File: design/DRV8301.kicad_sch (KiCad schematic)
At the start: 37 parts, among them U2 LM3671, U3 DRV8301

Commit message: Agregue LCSC Part #
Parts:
- L2: MPN LQM18DN220M70L -> (none); Manufacturer Murata Electronics -> APV
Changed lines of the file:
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@@
 			)
 		)
-		(property "Description" "600mA 2.2uH ±20% 300mΩ 0603 Inductors "
+		(property "Description" "600mA 2.2uH ±20% 300mΩ 0603 Inductors"
 			(at 120.65 147.32 0)
 			(effects
@@
 			)
 		)
-		(property "Manufacturer" "Murata Electronics"
+		(property "Manufacturer" "APV"
 			(at 194.31 50.8 0)
 			(effects
@@
 			)
 		)
-		(property "MPN" "LQM18DN220M70L"
+		(property "MPN" ""
 			(at 194.31 50.8 0)
 			(effects

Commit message: Agregue LCSC Part # a algunas resistencias
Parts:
- R10, R11, R9: LCSC (none) -> C163424
- R12, R14, R15: LCSC (none) -> C227479
- R13: LCSC (none) -> C6769250
- R4: LCSC (none) -> C108078
- R5: LCSC (none) -> C309650
- R6: LCSC (none) -> C114661
- R7: LCSC (none) -> C98220
- R8: LCSC (none) -> C123420
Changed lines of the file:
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@@
 			)
 		)
+		(property "LCSC" "C123420"
+			(at 119.38 29.21 0)
+			(effects
+				(font
+					(size 1.27 1.27)
+				)
+				(hide yes)
+			)
+		)
 		(pin "2"
 		)
@@
 			)
 		)
+		(property "LCSC" "C309650"
+			(at 85.09 36.83 0)
+			(effects
+				(font
+					(size 1.27 1.27)
+				)
+				(hide yes)
+			)
+		)
 		(pin "2"
 		)
@@
 			)
 		)
+		(property "LCSC" "C108078"
+			(at 85.09 26.67 0)
+			(effects
+				(font
+					(size 1.27 1.27)
+				)
+				(hide yes)
+			)
+		)
 		(pin "2"
 		)
@@
 			)
 		)
+		(property "LCSC" "C114661"
+			(at 99.06 35.56 0)
+			(effects
+				(font
+					(size 1.27 1.27)
+				)
+				(hide yes)
+			)
+		)
 		(pin "1"
 		)
@@
 			)
 		)
+		(property "LCSC" "C163424"
+			(at 240.03 101.6 0)
+			(effects
+				(font
+					(size 1.27 1.27)
+				)
+				(hide yes)
+			)
+		)
 		(pin "1"
 		)
@@
 			)
 		)
+		(property "LCSC" "C227479"
+			(at 250.19 106.68 0)
+			(effects
+				(font
+					(size 1.27 1.27)
+				)
+				(hide yes)
+			)
+		)
 		(pin "2"
 		)
@@
 			)
 		)
+		(property "LCSC" "C163424"
+			(at 240.03 119.38 0)
+			(effects
+				(font
+					(size 1.27 1.27)
+				)
+				(hide yes)
+			)
+		)
 		(pin "2"
 		)
@@
 			)
 		)
+		(property "LCSC" "C227479"
+			(at 250.19 121.92 0)
+			(effects
+				(font
+					(size 1.27 1.27)
+				)
+				(hide yes)
+			)
+		)
 		(pin "2"
 		)
@@
 			)
 		)
+		(property "LCSC" "C163424"
+			(at 240.03 142.24 0)
+			(effects
+				(font
+					(size 1.27 1.27)
+				)
+				(hide yes)
+			)
+		)
 		(pin "2"
 		)
@@
 			)
 		)
+		(property "LCSC" "C227479"
+			(at 240.03 147.32 0)
+			(effects
+				(font
+					(size 1.27 1.27)
+				)
+				(hide yes)
+			)
+		)
 		(pin "1"
 		)
@@
 			)
 		)
+		(property "LCSC" "C98220"
+			(at 107.95 53.34 0)
+			(effects
+				(font
+					(size 1.27 1.27)
+				)
+				(hide yes)
+			)
+		)
 		(pin "2"
 		)
@@
 			(at 248.92 41.91 0)
 			(effects
+				(font
+					(size 1.27 1.27)
+				)
+				(hide yes)
+			)
+		)
+		(property "LCSC" "C6769250"
+			(at 248.92 41.91 0)
+			(effects

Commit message: Correccion de DRC
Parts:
- U2: LCSC (none) -> C2650333
- U3: LCSC (none) -> C98969
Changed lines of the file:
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@@
+			)
+		)
+		(property "LCSC" "C98969"
+			(at 142.24 72.39 0)
+			(effects
+				(font
+					(size 1.27 1.27)
+				)
+				(hide yes)
 			)
 		)
@@
 			(at 101.6 149.86 0)
 			(effects
+				(font
+					(size 1.27 1.27)
+				)
+				(hide yes)
+			)
+		)
+		(property "LCSC" "C2650333"
+			(at 101.6 149.86 0)
+			(effects

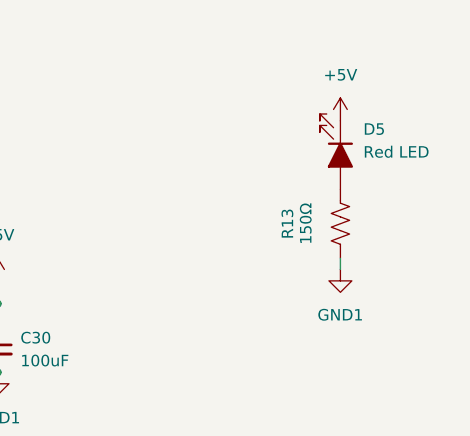
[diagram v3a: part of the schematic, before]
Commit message: Abaratando costos
Cambios en numeros de jlcpcb, pasados a componentes básicos
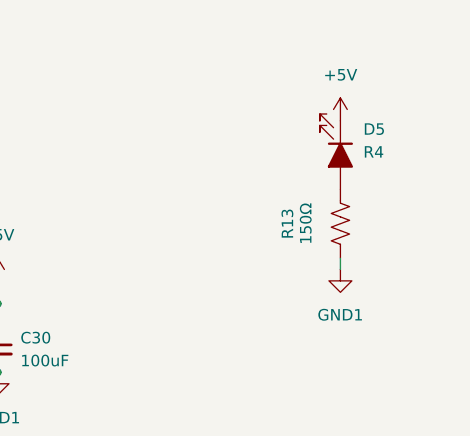
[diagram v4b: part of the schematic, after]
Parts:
- C15: footprint Capacitor_SMD:C_1206_3216Metric -> Capacitor_SMD:C_0603_1608Metric; LCSC C577236 -> C1631
- C19: LCSC C472763 -> C21122
- D5: value Red LED -> R4; LCSC C123009 -> C2286
- R10, R11, R9: LCSC C163424 -> C23153
- R12, R14, R15: LCSC C227479 -> C4190
- R13: LCSC C6769250 -> C22808
- R7: LCSC C98220 -> C25804
- R8: LCSC C123420 -> C22961
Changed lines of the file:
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@@
 			)
 		)
-		(property "LCSC" "C123420"
+		(property "LCSC" "C22961"
 			(at 119.38 29.21 0)
 			(effects
@@
 			)
 		)
-		(property "Footprint" "Capacitor_SMD:C_1206_3216Metric"
+		(property "Footprint" "Capacitor_SMD:C_0603_1608Metric"
 			(at 99.06 27.94 0)
 			(effects
@@
 			)
 		)
-		(property "Description" "CAP CER 6.8NF 1206"
+		(property "Description" "CAP CER 6.8NF 0603"
 			(at 99.06 27.94 0)
 			(effects
@@
 			)
 		)
-		(property "LCSC" "C577236"
+		(property "LCSC" "C1631"
 			(at 101.6 26.6762 0)
 			(effects
@@
 			)
 		)
-		(property "LCSC" "C472763"
+		(property "LCSC" "C21122"
 			(at 111.7536 64.77 0)
 			(effects
@@
 			)
 		)
-		(property "Value" "Red LED"
+		(property "Value" "R4"
 			(at 251.46 33.9724 90)
 			(effects
@@
 			)
 		)
-		(property "LCSC" "C123009"
+		(property "LCSC" "C2286"
 			(at 251.46 31.4324 0)
 			(effects
@@
 			)
 		)
-		(property "LCSC" "C163424"
+		(property "LCSC" "C23153"
 			(at 240.03 101.6 0)
 			(effects
@@
 			)
 		)
-		(property "LCSC" "C227479"
+		(property "LCSC" "C4190"
 			(at 250.19 106.68 0)
 			(effects
@@
 			)
 		)
-		(property "LCSC" "C163424"
+		(property "LCSC" "C23153"
 			(at 240.03 119.38 0)
 			(effects
@@
 			)
 		)
-		(property "LCSC" "C227479"
+		(property "LCSC" "C4190"
 			(at 250.19 121.92 0)
 			(effects
@@
 			)
 		)
-		(property "LCSC" "C163424"
+		(property "LCSC" "C23153"
 			(at 240.03 142.24 0)
 			(effects
@@
 			)
 		)
-		(property "LCSC" "C227479"
+		(property "LCSC" "C4190"
 			(at 240.03 147.32 0)
 			(effects
@@
 			)
 		)
-		(property "LCSC" "C98220"
+		(property "LCSC" "C25804"
 			(at 107.95 53.34 0)
 			(effects
@@
 			)
 		)
-		(property "LCSC" "C6769250"
+		(property "LCSC" "C22808"
 			(at 248.92 41.91 0)
 			(effects

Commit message: cambie resistencias a basic
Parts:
- D4: LCSC C6807777 -> C22452; MPN B260A -> SS54; Manufacturer FUXINSEMI -> MDD(Microdiode Semiconductor)
- R4: LCSC C108078 -> C22978; MPN RC0603FR-073K3L -> 0603WAF3301T5E; Manufacturer YAGEO -> UNI-ROYAL(Uniroyal Elec)
- R5: LCSC C309650 -> C25810; MPN RT0603BRD0718KL -> 0603WAF1802T5E; Manufacturer YAGEO -> UNI-ROYAL(Uniroyal Elec)
- R6: LCSC C114661 -> C22809; MPN RC0603FR-0715KL -> 0603WAF1502T5E; Manufacturer YAGEO -> UNI-ROYAL(Uniroyal Elec)
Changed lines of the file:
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@@
 			)
 		)
-		(property "Manufacturer" "YAGEO"
+		(property "Manufacturer" "UNI-ROYAL(Uniroyal Elec)"
 			(at 85.09 36.83 0)
 			(effects
@@
 			)
 		)
-		(property "MPN" "RT0603BRD0718KL"
+		(property "MPN" "0603WAF1802T5E"
 			(at 85.09 36.83 0)
 			(effects
@@
 			)
 		)
-		(property "LCSC" "C309650"
+		(property "LCSC" "C25810"
 			(at 85.09 36.83 0)
 			(effects
@@
 			)
 		)
-		(property "Manufacturer" "YAGEO"
+		(property "Manufacturer" "UNI-ROYAL(Uniroyal Elec)"
 			(at 85.09 26.67 0)
 			(effects
@@
 			)
 		)
-		(property "MPN" "RC0603FR-073K3L"
+		(property "MPN" "0603WAF3301T5E"
 			(at 85.09 26.67 0)
 			(effects
@@
 			)
 		)
-		(property "LCSC" "C108078"
+		(property "LCSC" "C22978"
 			(at 85.09 26.67 0)
 			(effects
@@
 			)
 		)
-		(property "Manufacturer" "YAGEO"
+		(property "Manufacturer" "UNI-ROYAL(Uniroyal Elec)"
 			(at 99.06 35.56 0)
 			(effects
@@
 			)
 		)
-		(property "MPN" "RC0603FR-0715KL"
+		(property "MPN" "0603WAF1502T5E"
 			(at 99.06 35.56 0)
 			(effects
@@
 			)
 		)
-		(property "LCSC" "C114661"
+		(property "LCSC" "C22809"
 			(at 99.06 35.56 0)
 			(effects
@@
 			)
 		)
-		(property "Description" "Shottky 60V 2A"
+		(property "Description" "40V Independent Type 550mV@5A 5A SMA(DO-214AC) Schottky Diodes ROHS"
 			(at 187.96 54.61 0)
 			(effects
@@
 			)
 		)
-		(property "Manufacturer" "FUXINSEMI"
+		(property "Manufacturer" "MDD(Microdiode Semiconductor)"
 			(at 187.96 54.61 0)
 			(effects
@@
 			)
 		)
-		(property "MPN" "B260A"
+		(property "MPN" "SS54"
 			(at 187.96 54.61 0)
 			(effects
@@
 			)
 		)
-		(property "LCSC" "C6807777"
+		(property "LCSC" "C22452"
 			(at 190.5 53.0224 0)
 			(effects

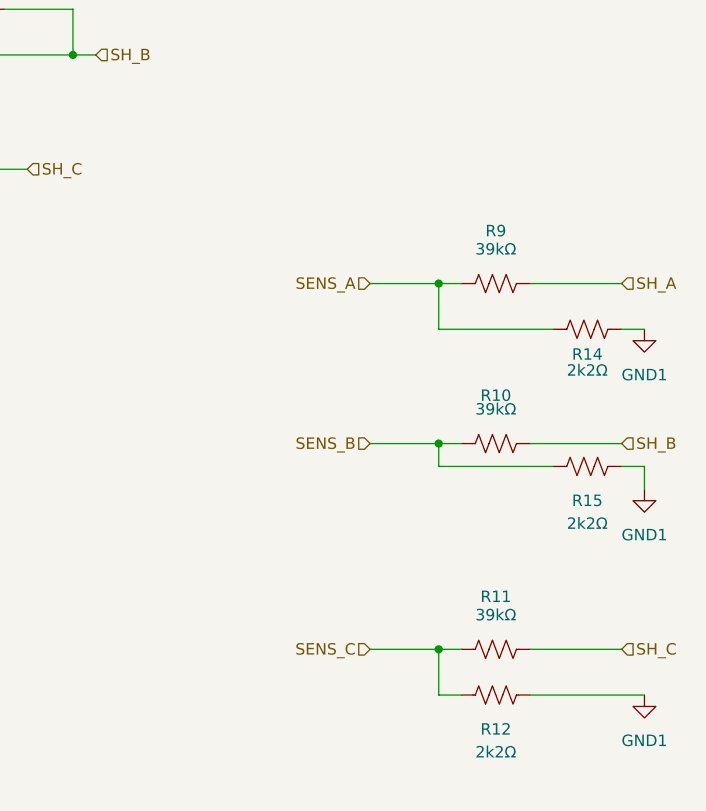
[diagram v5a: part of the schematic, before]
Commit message: Pequeños cambios finales
Agregado de test points, cambiado de algunos footprints, agregado de QR
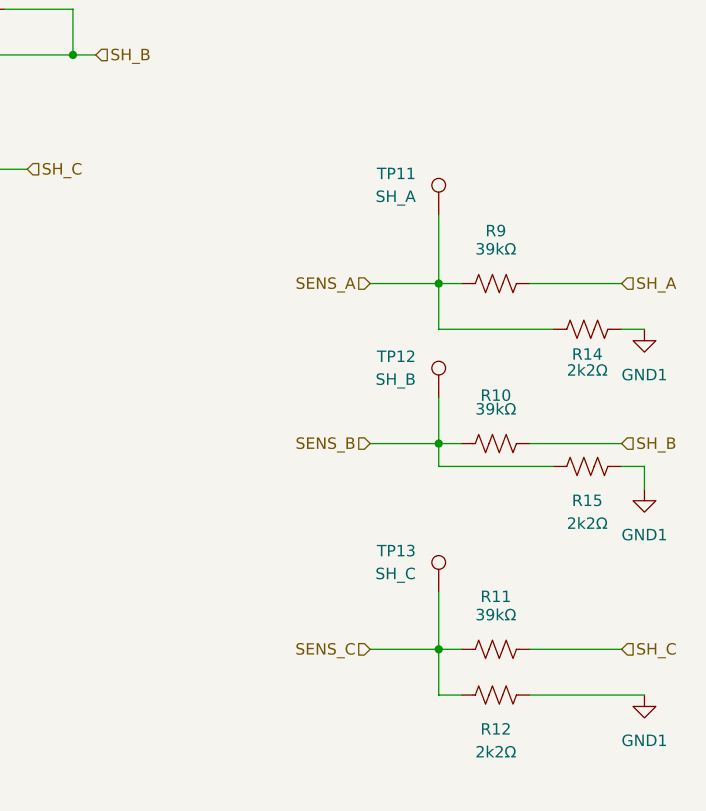
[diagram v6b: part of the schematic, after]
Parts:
- added TP11: SH_A, Connector_PinHeader_2.54mm:PinHeader_1x01_P2.54mm_Vertical, symbol Connector:TestPoint
- added TP12: SH_B, Connector_PinHeader_2.54mm:PinHeader_1x01_P2.54mm_Vertical, symbol Connector:TestPoint
- added TP13: SH_C, Connector_PinHeader_2.54mm:PinHeader_1x01_P2.54mm_Vertical, symbol Connector:TestPoint
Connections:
- net SENS_A: now also TP11.1
- net SENS_B: now also TP12.1
- net SENS_C: now also TP13.1
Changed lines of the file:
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@@
 	(wire
 		(pts
+			(xy 233.68 135.89) (xy 233.68 142.24)
+		)
+		(stroke
+			(width 0)
+			(type default)
+		)
+	)
+	(wire
+		(pts
 			(xy 162.56 76.2) (xy 193.04 76.2)
 		)
@@
 	(wire
 		(pts
+			(xy 233.68 114.3) (xy 233.68 119.38)
+		)
+		(stroke
+			(width 0)
+			(type default)
+		)
+	)
+	(wire
+		(pts
 			(xy 76.2 154.94) (xy 83.82 154.94)
 		)
@@
 	(wire
 		(pts
+			(xy 233.68 93.98) (xy 233.68 101.6)
+		)
+		(stroke
+			(width 0)
+			(type default)
+		)
+	)
+	(wire
+		(pts
 			(xy 182.88 63.5) (xy 187.96 63.5)
 		)
@@
 	)
 	(symbol
+		(lib_id "Connector:TestPoint")
+		(at 233.68 135.89 0)
+		(mirror y)
+		(unit 1)
+		(exclude_from_sim no)
+		(in_bom yes)
+		(on_board yes)
+		(dnp no)
+		(property "Reference" "TP13"
+			(at 231.14 131.3179 0)
+			(effects
+				(font
+					(size 1.27 1.27)
+				)
+				(justify left)
+			)
+		)
+		(property "Value" "SH_C"
+			(at 231.14 133.8579 0)
+			(effects
+				(font
+					(size 1.27 1.27)
+				)
+				(justify left)
+			)
+		)
+		(property "Footprint" "Connector_PinHeader_2.54mm:PinHeader_1x01_P2.54mm_Vertical"
+			(at 228.6 135.89 0)
+			(effects
+				(font
+					(size 1.27 1.27)
+				)
+				(hide yes)
+			)
+		)
+		(property "Datasheet" "~"
+			(at 228.6 135.89 0)
+			(effects
+				(font
+					(size 1.27 1.27)
+				)
+				(hide yes)
+			)
+		)
+		(property "Description" "test point"
+			(at 233.68 135.89 0)
+			(effects
+				(font
+					(size 1.27 1.27)
+				)
+				(hide yes)
+			)
+		)
+		(pin "1"
+		)
+		(instances
+			(project "ESCX"
+				(path "/6389d757-a1bd-4c0a-9d55-6114b19cc67a/00000000-0000-0000-0000-00005ae1478f"
+					(reference "TP13")
+					(unit 1)
+				)
+			)
+		)
+	)
+	(symbol
+		(lib_id "Connector:TestPoint")
+		(at 233.68 114.3 0)
+		(mirror y)
+		(unit 1)
+		(exclude_from_sim no)
+		(in_bom yes)
+		(on_board yes)
+		(dnp no)
+		(property "Reference" "TP12"
+			(at 231.14 109.7279 0)
+			(effects
+				(font
+					(size 1.27 1.27)
+				)
+				(justify left)
+			)
+		)
+		(property "Value" "SH_B"
+			(at 231.14 112.2679 0)
+			(effects
+				(font
+					(size 1.27 1.27)
+				)
+				(justify left)
+			)
+		)
+		(property "Footprint" "Connector_PinHeader_2.54mm:PinHeader_1x01_P2.54mm_Vertical"
+			(at 228.6 114.3 0)
+			(effects
+				(font
+					(size 1.27 1.27)
+				)
+				(hide yes)
+			)
+		)
+		(property "Datasheet" "~"
+			(at 228.6 114.3 0)
+			(effects
+				(font
+					(size 1.27 1.27)
+				)
+				(hide yes)
+			)
+		)
+		(property "Description" "test point"
+			(at 233.68 114.3 0)
+			(effects
+				(font
+					(size 1.27 1.27)
+				)
+				(hide yes)
+			)
+		)
+		(pin "1"
+		)
+		(instances
+			(project "ESCX"
+				(path "/6389d757-a1bd-4c0a-9d55-6114b19cc67a/00000000-0000-0000-0000-00005ae1478f"
+					(reference "TP12")
+					(unit 1)
+				)
+			)
+		)
+	)
+	(symbol
 		(lib_id "Device:R_US")
 		(at 248.92 41.91 0)
@@
 					(unit 1)
 				)
+			)
+		)
+	)
+	(symbol
+		(lib_id "Connector:TestPoint")
+		(at 233.68 93.98 0)
+		(mirror y)
+		(unit 1)
+		(exclude_from_sim no)
+		(in_bom yes)
+		(on_board yes)
+		(dnp no)
+		(property "Reference" "TP11"
+			(at 231.14 89.4079 0)
+			(effects
+				(font
+					(size 1.27 1.27)
+				)
+				(justify left)
+			)
+		)
+		(property "Value" "SH_A"
+			(at 231.14 91.9479 0)
+			(effects
+				(font
+					(size 1.27 1.27)
+				)
+				(justify left)
+			)
+		)
+		(property "Footprint" "Connector_PinHeader_2.54mm:PinHeader_1x01_P2.54mm_Vertical"
+			(at 228.6 93.98 0)
+			(effects
+				(font
+					(size 1.27 1.27)
+				)
+				(hide yes)
+			)
+		)
+		(property "Datasheet" "~"
+			(at 228.6 93.98 0)
+			(effects
+				(font
+					(size 1.27 1.27)
+				)
+				(hide yes)
+			)
+		)
+		(property "Description" "test point"
+			(at 233.68 93.98 0)
+			(effects
+				(font
+					(size 1.27 1.27)
+				)
+				(hide yes)
+			)
+		)
+		(pin "1"
+		)
+		(instances
+			(project "ESCX"
+				(path "/6389d757-a1bd-4c0a-9d55-6114b19cc67a/00000000-0000-0000-0000-00005ae1478f"
+					(reference "TP11")
+					(unit 1)
+				)

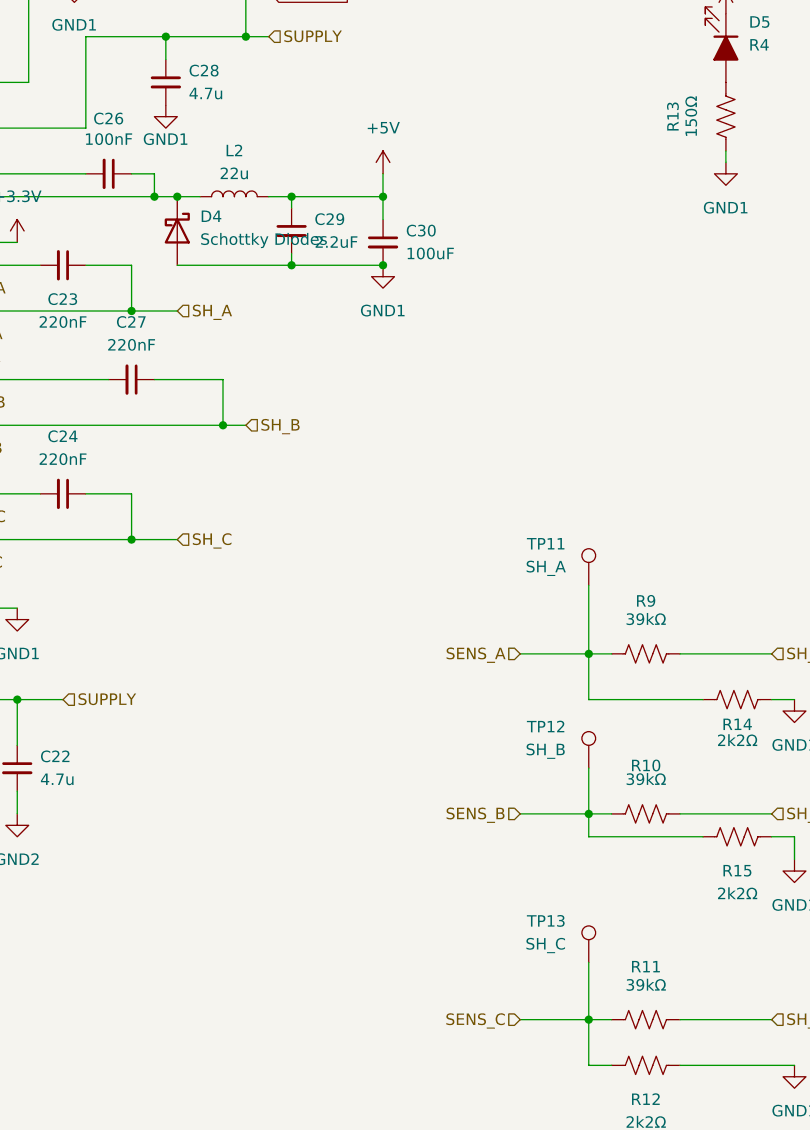
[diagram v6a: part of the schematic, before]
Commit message: cambios en la BOM
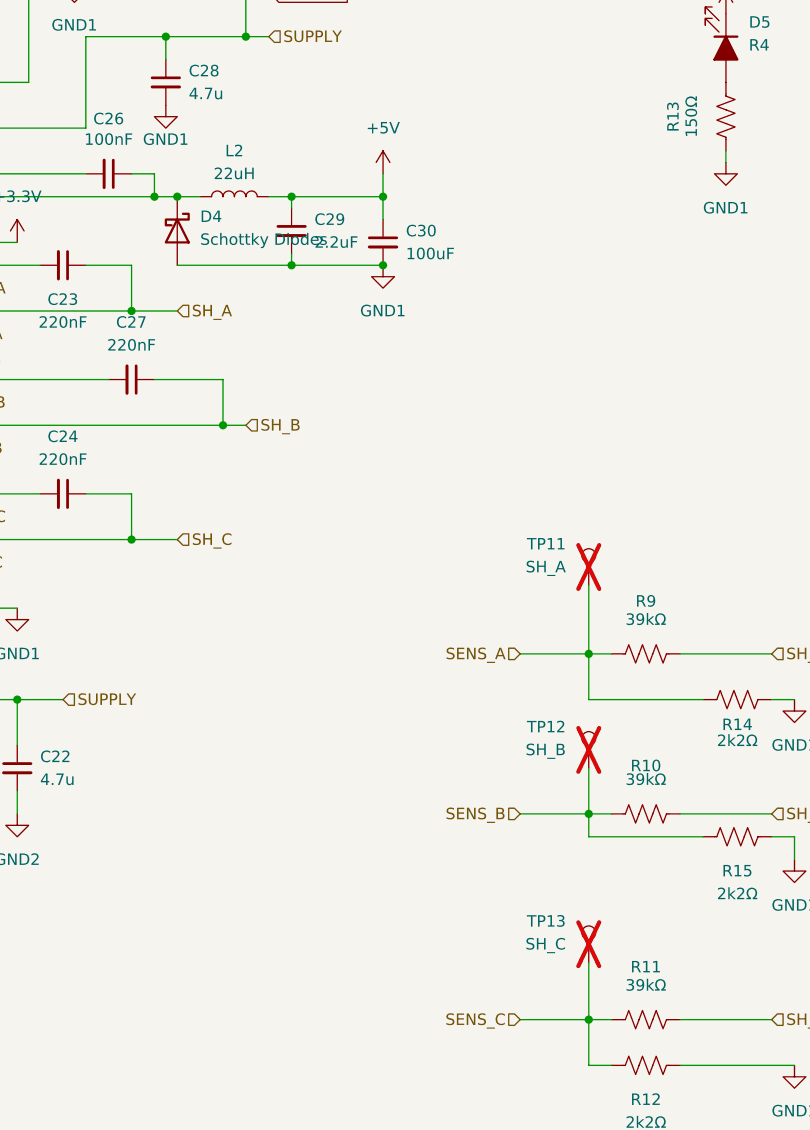
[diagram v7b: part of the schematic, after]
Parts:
- C12: footprint Capacitor_SMD:C_1210_3225Metric -> Capacitor_SMD:C_0603_1608Metric; LCSC C337978 -> C19666; MPN C1210X475K101T -> CL10A475KO8NNNC; Manufacturer Holy Stone Enterprise Co., Ltd. -> Samsung Electro-Mechanics
- L2: value 22u -> 22uH; MPN (none) -> AHW1608FE220KTF
- TP11, TP12, TP13: now not fitted
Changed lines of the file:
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@@
 			)
 		)
-		(property "Description" "600mA 2.2uH ±20% 300mΩ 0603 Inductors"
+		(property "Description" "600mA 2.2uH ±20% 300mΩ 0603"
 			(at 120.65 147.32 0)
 			(effects
@@
 			)
 		)
-		(property "Value" "22u"
+		(property "Value" "22uH"
 			(at 194.31 48.26 90)
 			(effects
@@
 			)
 		)
-		(property "Description" ""
+		(property "Description" "200mA 22uH ±10% 4.69Ω 0603"
 			(at 194.31 50.8 0)
 			(effects
@@
 			)
 		)
-		(property "MPN" ""
+		(property "MPN" "AHW1608FE220KTF"
 			(at 194.31 50.8 0)
 			(effects
@@
 			)
 		)
-		(property "Footprint" "Capacitor_SMD:C_1210_3225Metric"
+		(property "Footprint" "Capacitor_SMD:C_0603_1608Metric"
 			(at 76.2 149.86 0)
 			(effects
@@
 			)
 		)
-		(property "Description" "CAP CER 4.7UF 100V X7R 1210"
+		(property "Description" "CAP CER 4.7UF 16V X5R 0603"
 			(at 76.2 149.86 0)
 			(effects
@@
 			)
 		)
-		(property "Manufacturer" "Holy Stone Enterprise Co., Ltd. "
+		(property "Manufacturer" "Samsung Electro-Mechanics"
 			(at 76.2 149.86 0)
 			(effects
@@
 			)
 		)
-		(property "MPN" "C1210X475K101T"
+		(property "MPN" "CL10A475KO8NNNC"
 			(at 76.2 149.86 0)
 			(effects
@@
 			)
 		)
-		(property "LCSC" "C337978"
+		(property "LCSC" "C19666"
 			(at 78.74 148.5962 0)
 			(effects
@@
 		(in_bom yes)
 		(on_board yes)
-		(dnp no)
+		(dnp yes)
 		(property "Reference" "TP13"
 			(at 231.14 131.3179 0)
@@
 		(in_bom yes)
 		(on_board yes)
-		(dnp no)
+		(dnp yes)
 		(property "Reference" "TP12"
 			(at 231.14 109.7279 0)
@@
 		(in_bom yes)
 		(on_board yes)
-		(dnp no)
+		(dnp yes)
 		(property "Reference" "TP11"
 			(at 231.14 89.4079 0)
